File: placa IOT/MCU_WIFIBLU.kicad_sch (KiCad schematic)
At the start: 0 parts

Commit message: MICROCONTROLADOR EN PROCESO
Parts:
- added C10, C11: 0.1nF, Capacitor_SMD:C_0402_1005Metric, symbol Device:C
- added C12, C13: 12pF, Capacitor_SMD:C_0402_1005Metric, symbol Device:C
- added C14, C15, C16, C17, C18, C19: NC, Capacitor_SMD:C_0402_1005Metric, symbol Device:C
- added C5: 1uF, Capacitor_SMD:C_0402_1005Metric, symbol Device:C
- added C6, C8: 10nF, Capacitor_SMD:C_0402_1005Metric, symbol Device:C
- added C7: 100nF, Capacitor_SMD:C_0402_1005Metric, symbol Device:C
- added C9: 1nF, Capacitor_SMD:C_0402_1005Metric, symbol Device:C
- added L1: 2 mH, symbol Device:L
- added L2: 22 mH, symbol Device:L
- added R5: NC, Resistor_SMD:R_0402_1005Metric, symbol Device:R
- added R6: 499 OHM, Resistor_SMD:R_0402_1005Metric, symbol Device:R
- added U3: ESP32-S3, ic_control:QFN-56-1EP_7x7mm_P0.4mm_EP4x4mm, symbol ic_control:ESP32-S3
- added U4: PRO-OB-536, antennas:ANTENNA_PIFA_3D_2.4GHZ, symbol antennas:ANTENNA_PIFA_3D_2.4GHZ
- added Y1: 40 MHz, Crystal:Crystal_SMD_3225-4Pin_3.2x2.5mm, symbol Device:Crystal_GND24
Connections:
- new net: C14.2, C16.1, C17.1, C18.1
- new net: C14.1, C15.1, U3.1 (LNA_IN)
- new net: C18.2, C19.1, U4.2 (FEED)
- new net: C11.1, L1.2, U3.2 (VDD3P3), U3.3 (VDD3P3)
- new net: C12.1, L2.1, Y1.1
- new net: C13.1, U3.53 (XTAL_N), Y1.3
- new net: L2.2, U3.54 (XTAL_P)
- new net: R6.2, U3.49 (U0TXD)
- new net +3.3V: C10.1, C5.1, C6.1, C7.1, C8.1, C9.1, L1.1, R5.2, U3.46 (VDD3P3_CPU), U3.55 (VDDA), U3.56 (VDDA)
- new net GND: C10.2, C11.2, C12.2, C13.2, C15.2, C16.2, C17.2, C19.2, C5.2, C6.2, C7.2, C8.2, C9.2, U3.57 (GND), U4.1 (GND), Y1.2 (G), Y1.4 (G)
- new net IO42/MTMS: U3.48 (MTMS)
- new net IO45: R5.1, U3.51 (GPIO45)
- new net IO46: U3.52 (GPIO46)
- new net RST/EN: U3.4 (CHIP_PU)
- new net SD0-MISO-IO2: U3.7 (GPIO2)
- new net U0RXD: U3.50 (U0RXD)
- new net U0TXD: R6.1
- no-connect marks 0 -> 7

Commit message: MICROCONTROLADOR TERMINADO
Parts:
- added C20: 100nF, Capacitor_SMD:C_0402_1005Metric, symbol Device:C
- added C21: 1uF, Capacitor_SMD:C_0402_1005Metric, symbol Device:C
- added J1, J2: 22-28-4144, connectors:CONN_THT_MV_PH_P2.54MM_P14, symbol connectors:CONN_THT_MV_PH_P2.54MM_P14
- added R8, R9: 10K, Resistor_SMD:R_0402_1005Metric, symbol Device:R
- added SW1: RST/EN, Button_Switch_SMD:SW_Push_SPST_NO_Alps_SKRK, symbol Switch:SW_Push
- added SW2: BOOT, Button_Switch_SMD:SW_Push_SPST_NO_Alps_SKRK, symbol Switch:SW_Push
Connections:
- net +3.3V: now also U3.20 (VDD3P3_RTC), C20.1, J1.3 (Pin_3), R8.2, R9.2
- net GND: now also C20.2, C21.2, J1.2 (Pin_2), J1.4 (Pin_4), J2.14 (Pin_14), SW1.1, SW2.1
- net IO42/MTMS: now also J1.5 (Pin_5)
- net IO45: now also J1.7 (Pin_7)
- net IO46: now also J1.6 (Pin_6)
- net RST/EN: now also C21.1, J2.11 (Pin_11), R8.1, SW1.2
- net U0RXD: now also J1.11 (Pin_11)
- net U0TXD: now also J1.12 (Pin_12)
- net IO5: now reaches U3.10 (GPIO5)
- net IO6: now reaches U3.11 (GPIO6)
- net IO7: now reaches U3.12 (GPIO7)
- net IO8: now reaches U3.13 (GPIO8)
- net IO8: now also J2.9 (Pin_9)
- net IO9: now reaches U3.14 (GPIO9)
- net LORA_TX: now reaches U3.15 (GPIO10)
- net CMD-M0S1-IO11: now reaches U3.16 (GPIO11)
- net ID12: now reaches U3.17 (GPIO12)
- net SD3-CS-IO13: now reaches U3.18 (GPIO13)
- net CLK-SCK-IO14: now reaches U3.19 (GPIO14)
- net IO15: now reaches U3.21 (XTAL_32K_P)
- net IO15: now also J2.12 (Pin_12)
- net IO16: now reaches U3.22 (XTAL_32K_N)
- net IO16: now also J2.13 (Pin_13)
- net ID17: now reaches U3.23 (GPIO17)
- net ID18: now reaches U3.24 (GPIO18)
- net DM: now reaches U3.25 (GPIO19/USB_D-)
- net DP: now reaches U3.26 (GPIO20/USB_D+)
- net LORA_RX: now reaches U3.27 (GPIO21)
- net IO48: now reaches U3.36 (SPICLK_N)
- net IO48: now also J2.8 (Pin_8)
- net IO47: now reaches U3.37 (SPICLK_P)
- net IO47: now also J2.7 (Pin_7)
- net IO33: now reaches U3.38 (GPIO33)
- net IO33: now also J2.6 (Pin_6)
- net IO34: now reaches U3.39 (GPIO34)
- net IO34: now also J2.5 (Pin_5)
- net IO35: now reaches U3.40 (GPIO35)
- net IO36: now reaches U3.41 (GPIO36)
- net IO36: now also J2.2 (Pin_2)
- net IO37: now reaches U3.42 (GPIO37)
- net IO37: now also J2.1 (Pin_1)
- net IO39/MTCK: now reaches U3.44 (MTCK)
- net IO39/MTCK: now also U3.45 (MTDO), J1.10 (Pin_10)
- net IO0: now reaches U3.5 (GPIO0)
- net IO0: now also J2.3 (Pin_3)
- net IO1: now reaches U3.6 (GPIO1)
- net IO3: now reaches U3.8 (GPIO3)
- net IO4: now reaches U3.9 (GPIO4)
- new net ID0: R9.1, SW2.2
- new net IO12: J2.10 (Pin_10)
- new net IO38: J1.13 (Pin_13)
- new net IO40/MTDO: J1.9 (Pin_9)
- new net IO41/MTDI: J1.8 (Pin_8)
- new net O35: J2.4 (Pin_4)
- new net VBAT: J1.14 (Pin_14)
- new net VBUS: J1.1 (Pin_1)
- no-connect marks 7 -> 8
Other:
- moved on the sheet: R5

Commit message: RF TERMINADO
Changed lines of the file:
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@@
 		(dnp no)
 		(property "Reference" "C15"
-			(at 275.59 189.2299 0)
+			(at 266.7 189.992 0)
 			(show_name no)
 			(do_not_autoplace no)
@@
 		)
 		(property "Value" "NC"
-			(at 275.59 191.7699 0)
+			(at 267.97 192.786 0)
 			(show_name no)
 			(do_not_autoplace no)

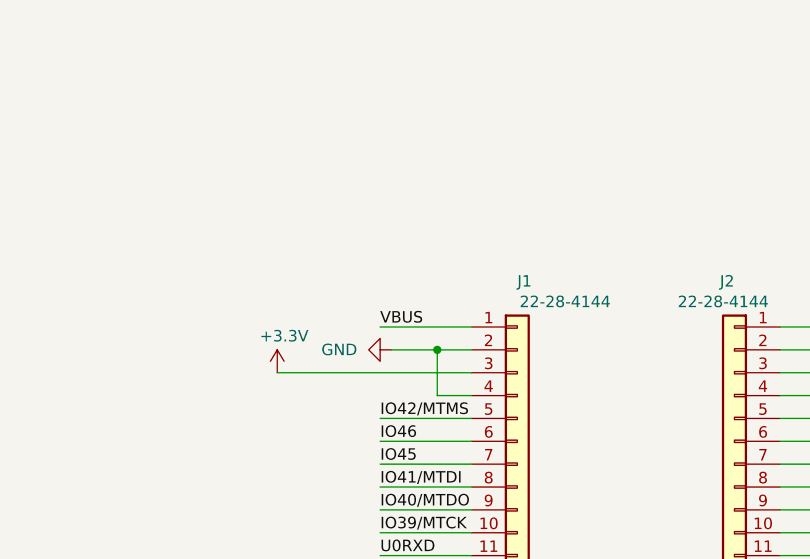
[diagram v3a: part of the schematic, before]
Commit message: MICROCONTROLADOR TERMINADOCON CAMBIO
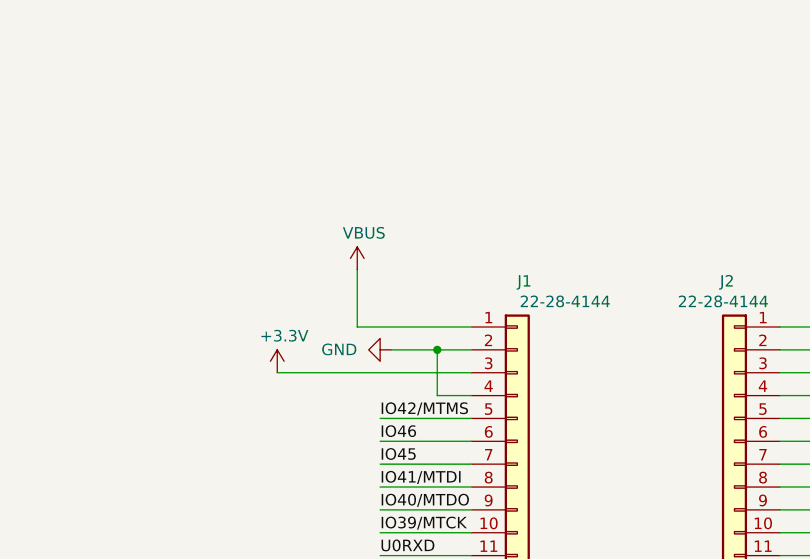
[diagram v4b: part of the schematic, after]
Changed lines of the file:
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@@
 	(wire
 		(pts
+			(xy 323.85 63.5) (xy 336.55 63.5)
+		)
+		(stroke
+			(width 0)
+			(type default)
+		)
+	)
+	(wire
+		(pts
 			(xy 194.31 181.61) (xy 149.86 181.61)
 		)
@@
 	(wire
 		(pts
+			(xy 323.85 57.15) (xy 323.85 63.5)
+		)
+		(stroke
+			(width 0)
+			(type default)
+		)
+	)
+	(wire
+		(pts
 			(xy 241.3 158.75) (xy 255.27 158.75)
 		)
@@
 	(wire
 		(pts
-			(xy 326.39 63.5) (xy 336.55 63.5)
-		)
-		(stroke
-			(width 0)
-			(type default)
-		)
-	)
-	(wire
-		(pts
 			(xy 194.31 138.43) (xy 177.8 138.43)
 		)
@@
 		)
 	)
-	(label "VBUS"
-		(at 326.39 63.5 0)
-		(effects
-			(font
-				(size 1.27 1.27)
-			)
-			(justify left bottom)
-		)
-	)
 	(label "IO6"
 		(at 177.8 138.43 0)
@@
 					(unit 1)
 				)
+			)
+		)
+	)
+	(symbol
+		(lib_id "power:+3.3V")
+		(at 323.85 57.15 0)
+		(unit 1)
+		(body_style 1)
+		(exclude_from_sim no)
+		(in_bom yes)
+		(on_board yes)
+		(in_pos_files yes)
+		(dnp no)
+		(property "Reference" "#PWRVBUS"
+			(at 323.85 60.96 0)
+			(hide yes)
+			(show_name no)
+			(do_not_autoplace no)
+			(effects
+				(font
+					(size 1.27 1.27)
+				)
+			)
+		)
+		(property "Value" "VBUS"
+			(at 324.612 53.086 0)
+			(show_name no)
+			(do_not_autoplace no)
+			(effects
+				(font
+					(size 1.27 1.27)
+				)
+			)
+		)
+		(property "Footprint" ""
+			(at 323.85 57.15 0)
+			(hide yes)
+			(show_name no)
+			(do_not_autoplace no)
+			(effects
+				(font
+					(size 1.27 1.27)
+				)
+			)
+		)
+		(property "Datasheet" ""
+			(at 323.85 57.15 0)
+			(hide yes)
+			(show_name no)
+			(do_not_autoplace no)
+			(effects
+				(font
+					(size 1.27 1.27)
+				)
+			)
+		)
+		(property "Description" "Power symbol creates a global label with name \"+3.3V\""
+			(at 323.85 57.15 0)
+			(hide yes)
+			(show_name no)
+			(do_not_autoplace no)
+			(effects
+				(font
+					(size 1.27 1.27)
+				)
+			)
+		)
+		(pin "1"
+		)
+		(instances
+			(project "placa IOT"
+				(path "/fbbb61cd-c6c4-4d51-9fb8-e36c0f4e7910/b110d936-1717-4256-b0de-00c7e20cfda6"
+					(reference "#PWRVBUS")
+					(unit 1)
+				)

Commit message: USB TERMINADO
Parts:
- added D6: LED GREEN, symbol Device:LED
- added R23: 2K OHM, Resistor_SMD:R_0402_1005Metric, symbol Device:R
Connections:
- net GND: now also D6.1 (K)
- net IO37: now also R23.2
- new net: D6.2 (A), R23.1

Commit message: ACABADO
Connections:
- net DM renamed D+
- net DP renamed D-
- net IO1 renamed ID1
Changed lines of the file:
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@@
+		)
+	)
+	(hierarchical_label "D-"
+		(shape input)
+		(at 177.8 168.91 180)
+		(effects
+			(font
+				(size 1.27 1.27)
+			)
+			(justify right)
+		)
+	)
+	(hierarchical_label "IO9"
+		(shape output)
+		(at 177.8 146.05 180)
+		(effects
+			(font
+				(size 1.27 1.27)
+			)
+			(justify right)
+		)
+	)
+	(hierarchical_label "LORA_TX"
+		(shape output)
+		(at 177.8 148.59 0)
+		(effects
+			(font
+				(size 1.27 1.27)
+			)
+			(justify left)
+		)
+	)
+	(hierarchical_label "ID1"
+		(shape input)
+		(at 177.8 125.73 0)
+		(effects
+			(font
+				(size 1.27 1.27)
+			)
+			(justify left)
+		)
+	)
+	(hierarchical_label "IO33"
+		(shape output)
+		(at 255.27 146.05 0)
+		(effects
+			(font
+				(size 1.27 1.27)
+			)
+			(justify left)
+		)
+	)
+	(hierarchical_label "IO8"
+		(shape output)
+		(at 177.8 143.51 180)
+		(effects
+			(font
+				(size 1.27 1.27)
+			)
+			(justify right)
+		)
+	)
+	(hierarchical_label "IO7"
+		(shape output)
+		(at 177.8 140.97 180)
+		(effects
+			(font
+				(size 1.27 1.27)
+			)
+			(justify right)
+		)
+	)
+	(hierarchical_label "IO34"
+		(shape output)
+		(at 255.27 148.59 0)
+		(effects
+			(font
+				(size 1.27 1.27)
+			)
+			(justify left)
+		)
+	)
+	(hierarchical_label "IO3"
+		(shape output)
+		(at 177.8 130.81 180)
+		(effects
+			(font
+				(size 1.27 1.27)
+			)
+			(justify right)
+		)
+	)
+	(hierarchical_label "IO5"
+		(shape output)
+		(at 177.8 135.89 180)
+		(effects
+			(font
+				(size 1.27 1.27)
+			)
+			(justify right)
+		)
+	)
+	(hierarchical_label "IO4"
+		(shape input)
+		(at 177.8 133.35 180)
+		(effects
+			(font
+				(size 1.27 1.27)
+			)
+			(justify right)
+		)
+	)
+	(hierarchical_label "IO36"
+		(shape bidirectional)
+		(at 255.27 153.67 180)
+		(effects
+			(font
+				(size 1.27 1.27)
+			)
+			(justify right)
+		)
+	)
+	(hierarchical_label "LORA_RX"
+		(shape output)
+		(at 177.8 171.45 0)
+		(effects
+			(font
+				(size 1.27 1.27)
+			)
+			(justify left)
+		)
+	)
+	(hierarchical_label "IO6"
+		(shape output)
+		(at 177.8 138.43 180)
+		(effects
+			(font
+				(size 1.27 1.27)
+			)
+			(justify right)
+		)
+	)
+	(hierarchical_label "D+"
+		(shape input)
+		(at 177.8 166.37 180)
+		(effects
+			(font
+				(size 1.27 1.27)
+			)
+			(justify right)
 		)
 	)

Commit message: ULTIMA  PRUEBA
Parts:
- D6: footprint (none) -> LED_SMD:LED_0402_1005Metric
- L1, L2: footprint (none) -> Inductor_SMD:L_0402_1005Metric
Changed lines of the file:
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@@
 	(wire
 		(pts
+			(xy 269.24 171.45) (xy 266.7 171.45)
+		)
+		(stroke
+			(width 0)
+			(type default)
+		)
+	)
+	(wire
+		(pts
 			(xy 154.94 85.09) (xy 167.64 85.09)
 		)
@@
 	)
 	(label "U0TXD"
-		(at 266.7 171.45 0)
+		(at 269.24 171.45 0)
 		(effects
 			(font
@@
 			)
 		)
-		(property "Footprint" ""
+		(property "Footprint" "LED_SMD:LED_0402_1005Metric"
 			(at 311.15 156.21 0)
 			(hide yes)
@@
 		(in_pos_files yes)
 		(dnp no)
-		(property "Reference" "#PWRVBUS"
+		(property "Reference" "#PWRVBUS03"
 			(at 323.85 60.96 0)
 			(hide yes)
@@
 			(project "placa IOT"
 				(path "/fbbb61cd-c6c4-4d51-9fb8-e36c0f4e7910/b110d936-1717-4256-b0de-00c7e20cfda6"
-					(reference "#PWRVBUS")
+					(reference "#PWRVBUS03")
 					(unit 1)
 				)
@@
 			)
 		)
-		(property "Footprint" ""
+		(property "Footprint" "Inductor_SMD:L_0402_1005Metric"
 			(at 187.96 85.09 0)
 			(hide yes)
@@
 			)
 		)
-		(property "Footprint" ""
+		(property "Footprint" "Inductor_SMD:L_0402_1005Metric"
 			(at 149.86 190.5 0)
 			(hide yes)
@@
 		(in_pos_files yes)
 		(dnp no)
-		(property "Reference" "#PWRVBAT"
+		(property "Reference" "#PWRVBAT05"
 			(at 318.77 100.33 0)
 			(hide yes)
@@
 			(project "placa IOT"
 				(path "/fbbb61cd-c6c4-4d51-9fb8-e36c0f4e7910/b110d936-1717-4256-b0de-00c7e20cfda6"
-					(reference "#PWRVBAT")
+					(reference "#PWRVBAT05")
 					(unit 1)
 				)
